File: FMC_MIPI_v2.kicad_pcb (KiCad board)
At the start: 6 copper layers, 69 x 112 mm, 99 parts, among them IC2 AT24MAC402-MAHM-T, IC3 TCA9406DCUR, J1 ASP-134488-01, J2 QTH-060-01-L-D-A, U1 LP5907MFX-1.8, U2 SN74AVC2T45DCUR, U3 SN74AVCH16T245_DGV_48, U4 TLV75525PDBV, U5 TS3DDR3812_RUA_42, U6 TS3DDR3812_RUA_42, U7 LP5907MFX-1.2, U8 SN74AVCH16T245_DGV_48

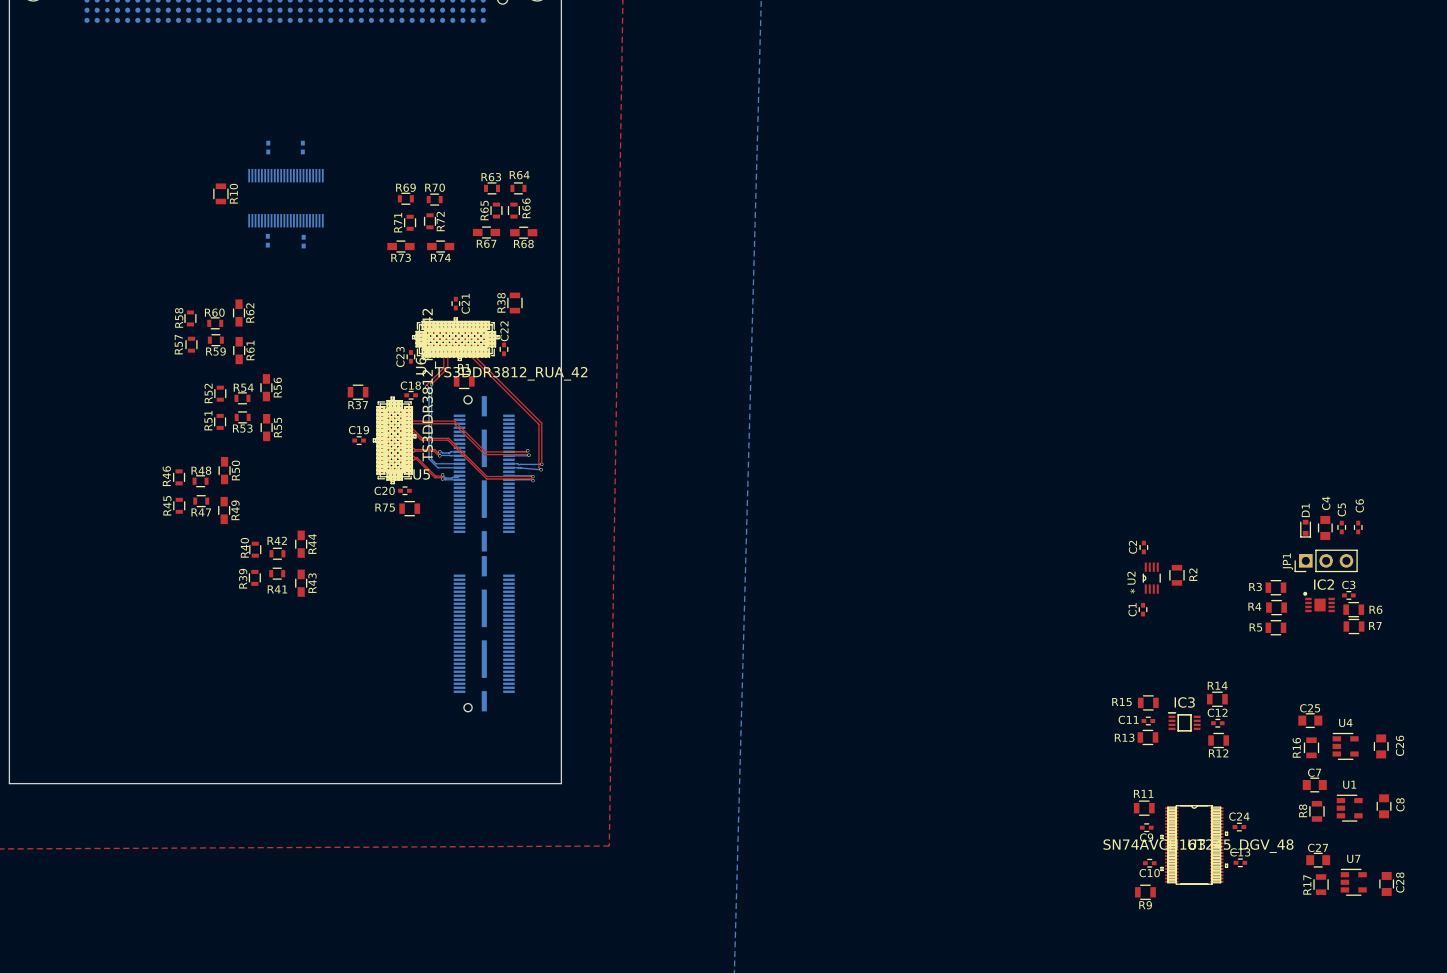
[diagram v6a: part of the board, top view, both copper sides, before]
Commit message: added 4 bit level shifter VADJ to 3.3 volt
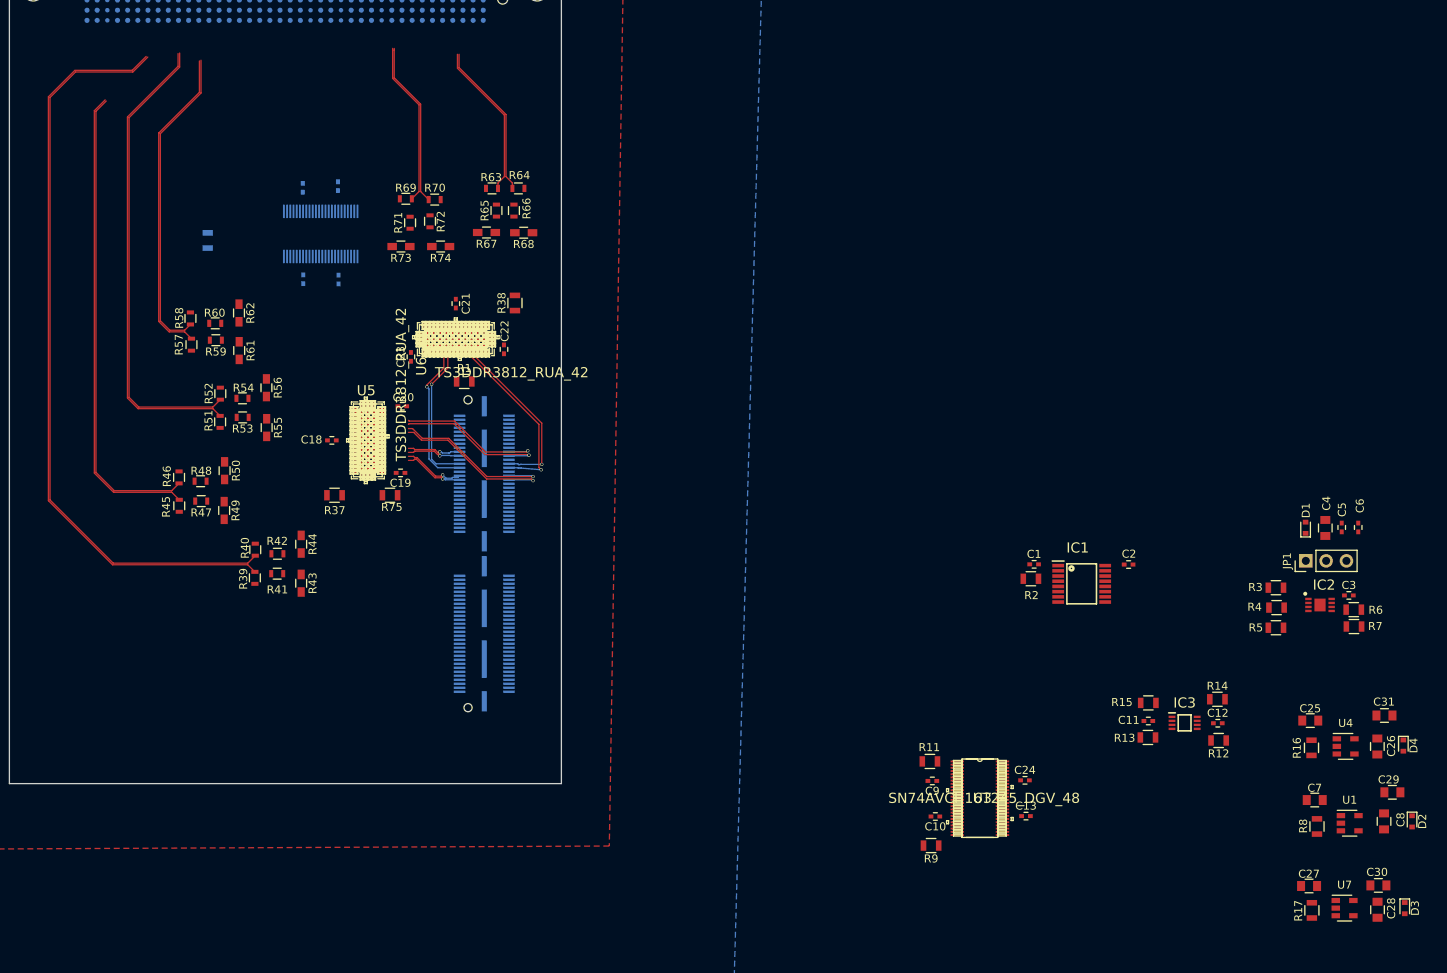
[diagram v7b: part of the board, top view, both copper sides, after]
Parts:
- removed U2: SN74AVC2T45DCUR, FMC_MIPI_v2_sym:SN74AVC2T45DCUR
- added C29: 4.7uF, Capacitors_SMD:C_0805, F.Cu at (263.4, 142.1)
- added C30: 4.7uF, Capacitors_SMD:C_0805, F.Cu at (261.6, 153.7)
- added C31: 4.7uF, Capacitors_SMD:C_0805, F.Cu at (262.4, 132.5)
- added D2: UCLAMP0501H.TCT, Diodes_SMD:D_SOD-523, F.Cu at (265.8, 145.7)
- added D3: UCLAMP0501H.TCT, Diodes_SMD:D_SOD-523, F.Cu at (264.9, 156.6)
- added D4: UCLAMP0501H.TCT, Diodes_SMD:D_SOD-523, F.Cu at (264.7, 136.2)
- added IC1: SN74AVC4T245PWR, SOP65P640X120-16N, F.Cu at (224.5, 116.0)
- R10: moved to B.Cu
- moved C10 27.4 mm to (206.2, 145.1)
- moved C24 27.4 mm to (217.4, 140.6)
- moved C9 27.4 mm to (205.9, 140.7)
- moved R11 27.4 mm to (205.6, 138.2)
- moved U3 27.4 mm to (211.8, 142.8)
- moved C13 27.4 mm to (217.6, 145.1)
- moved R9 27.4 mm to (205.7, 148.7)
- moved R2 18.3 mm to (218.2, 115.4), turned to 0 degrees
- moved C1 14.7 mm to (218.6, 113.6), turned to 0 degrees
- moved R37 13.2 mm to (131.1, 105.0), turned to 0 degrees
- moved C18 11.4 mm to (130.8, 98.1), turned to 0 degrees
- moved C20 10.6 mm to (139.6, 93.8), turned to 180 degrees
- moved C14 9.96 mm to (131.6, 66.3)
- moved C19 6.57 mm to (139.4, 102.2), turned to 180 degrees
- moved C16 6.54 mm to (127.2, 78.0)
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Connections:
- R2 pad 2: /LVDS_to_Jetson_lines/DIR_U2 -> /LVDS_to_Jetson_lines/DIR_IC1
- R37 pad 1: /LVDS_to_Jetson_lines/EN -> /LVDS_to_Jetson_lines/EN_U5
- R37 pad 2: /VOLT_3P3 -> /LVDS_to_Jetson_lines/EN_MIPI_OUT_DATA_3V3
- R38 pad 1: /LVDS_to_Jetson_lines/EN -> /LVDS_to_Jetson_lines/EN_U6
- R38 pad 2: /VOLT_3P3 -> /LVDS_to_Jetson_lines/EN_MIPI_OUT_CLOCK_3V3
- U5 pad 8: /LVDS_to_Jetson_lines/EN -> /LVDS_to_Jetson_lines/EN_U5
- U6 pad 8: /LVDS_to_Jetson_lines/EN -> /LVDS_to_Jetson_lines/EN_U6
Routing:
- net /LVDS_to_Jetson_lines/FMC_HS_CSI_C_D1_N: track 0.00 -> 94.3 mm
- net /LVDS_to_Jetson_lines/FMC_HS_CSI_C_D1_P: track 0.00 -> 93.9 mm
- net /LVDS_to_Jetson_lines/FMC_HS_CSI_C_D0_N: track 0.00 -> 59.2 mm
- net /LVDS_to_Jetson_lines/FMC_HS_CSI_C_D0_P: track 0.00 -> 58.7 mm
- net /LVDS_to_Jetson_lines/FMC_HS_CSI_D_D1_N: track 0.00 -> 58.2 mm
- net /LVDS_to_Jetson_lines/FMC_HS_CSI_D_D1_P: track 0.00 -> 58.0 mm
- net /LVDS_to_Jetson_lines/FMC_HS_CSI_D_D0_N: track 0.00 -> 39.6 mm
- net /LVDS_to_Jetson_lines/FMC_HS_CSI_D_D0_P: track 0.00 -> 39.2 mm
- net /LVDS_to_Jetson_lines/FMC_HS_CSI_C_CLK_P: track 0.00 -> 20.7 mm
- net /LVDS_to_Jetson_lines/FMC_HS_CSI_C_CLK_N: track 0.00 -> 20.5 mm
- net /LVDS_to_Jetson_lines/FMC_HS_CSI_D_CLK_P: track 0.00 -> 19.5 mm
- net /LVDS_to_Jetson_lines/FMC_HS_CSI_D_CLK_N: track 0.00 -> 19.5 mm

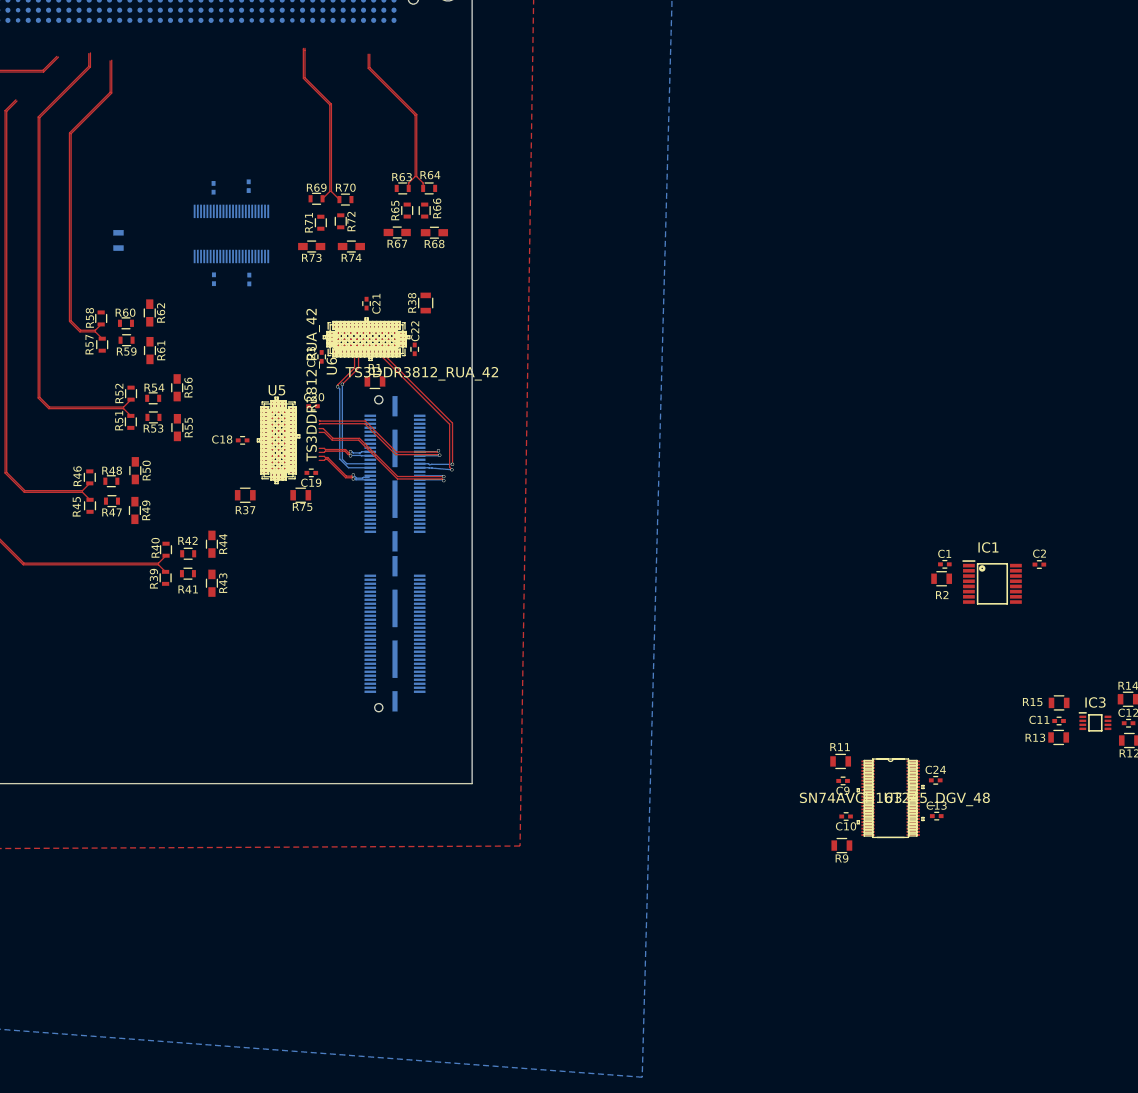
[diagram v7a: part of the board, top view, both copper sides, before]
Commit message: added enable line for slow signals
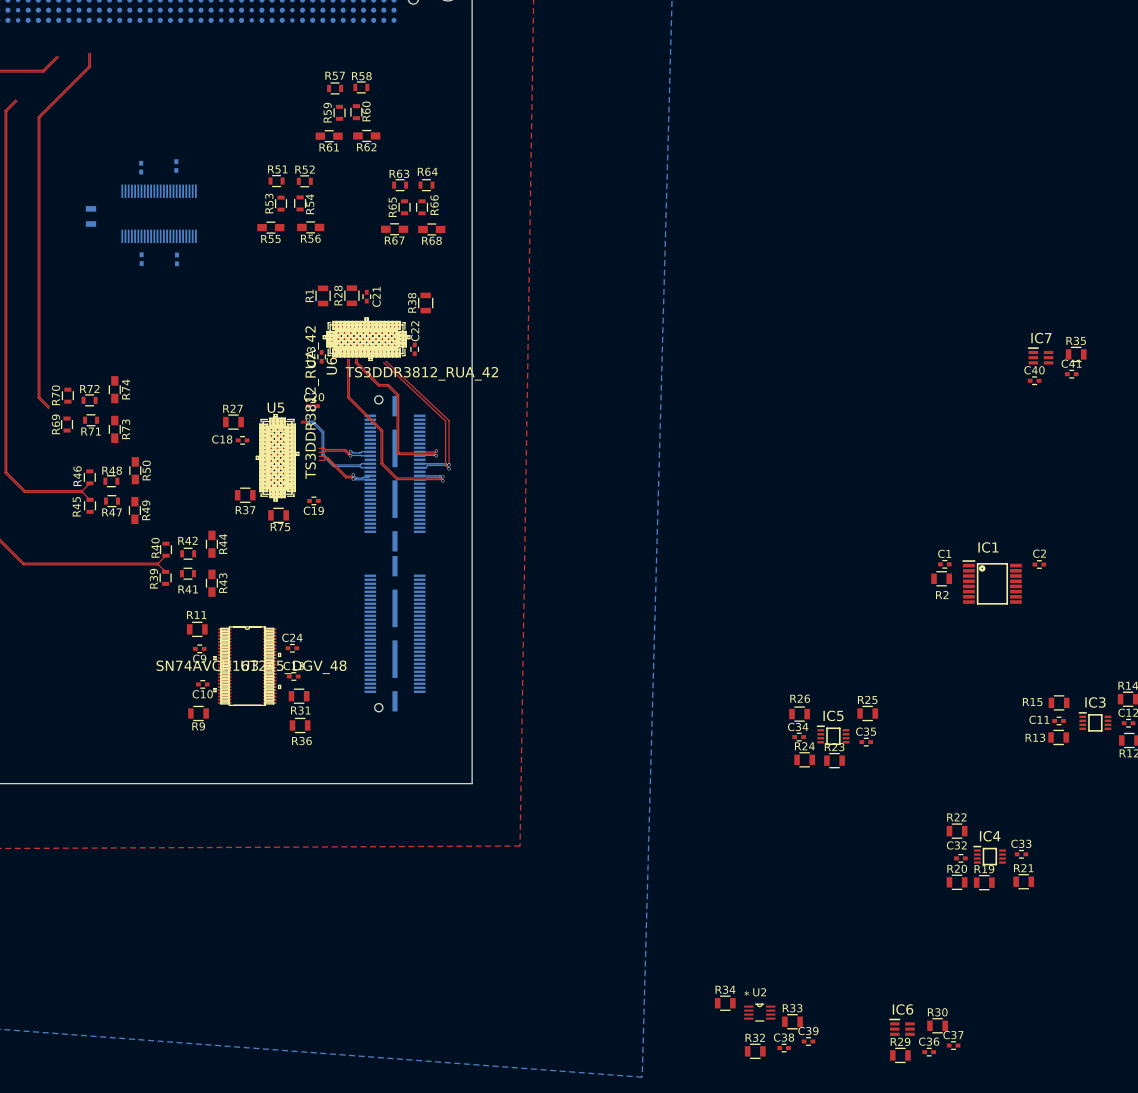
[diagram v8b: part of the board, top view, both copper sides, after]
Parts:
- added C32: 0.1uF, Capacitors_SMD:C_0402, F.Cu at (220.6, 150.3)
- added C33: 0.1uF, Capacitors_SMD:C_0402, F.Cu at (228.2, 149.8)
- added C34: 0.1uF, Capacitors_SMD:C_0402, F.Cu at (200.4, 135.2)
- added C35: 0.1uF, Capacitors_SMD:C_0402, F.Cu at (208.8, 135.8)
- added C36: 0.1uF, Capacitors_SMD:C_0402, F.Cu at (216.6, 174.6)
- added C37: 0.1uF, Capacitors_SMD:C_0402, F.Cu at (219.7, 173.7)
- added C38: 0.1uF, Capacitors_SMD:C_0402, F.Cu at (198.5, 174.1)
- added C39: 0.1uF, Capacitors_SMD:C_0402, F.Cu at (201.5, 173.2)
- added C40: 0.1uF, Capacitors_SMD:C_0402, F.Cu at (229.8, 90.6)
- added C41: 0.1uF, Capacitors_SMD:C_0402, F.Cu at (234.5, 89.8)
- added IC4: TCA9406DCUR, FMC_MIPI_v2_sym:SOP50P310X90-8N, F.Cu at (224.2, 150.1)
- added IC5: TCA9406DCUR, FMC_MIPI_v2_sym:SOP50P310X90-8N, F.Cu at (204.7, 135.1)
- added IC6: SN74AVC1T45DCKT, FMC_MIPI_v2_sym:SOT65P210X110-6N, F.Cu at (213.3, 171.7)
- added IC7: SN74AVC1T45DCKT, FMC_MIPI_v2_sym:SOT65P210X110-6N, F.Cu at (230.6, 87.8)
- added R19: 0, Resistors_SMD:R_0805, F.Cu at (223.5, 153.4)
- added R20: 0, Resistors_SMD:R_0805, F.Cu at (220.1, 153.3)
- added R21: 0, Resistors_SMD:R_0805, F.Cu at (228.4, 153.3)
- added R22: 0, Resistors_SMD:R_0805, F.Cu at (220.1, 146.9)
- added R23: 0, Resistors_SMD:R_0805, F.Cu at (204.8, 138.1)
- added R24: 0, Resistors_SMD:R_0805, F.Cu at (201.1, 138.0)
- added R25: 0, Resistors_SMD:R_0805, F.Cu at (208.9, 132.2)
- added R26: 0, Resistors_SMD:R_0805, F.Cu at (200.4, 132.3)
- added R27: 0, Resistors_SMD:R_0805, F.Cu at (129.7, 95.8)
- added R28: 0, Resistors_SMD:R_0805, F.Cu at (144.5, 80.0)
- added R29: 1k, Resistors_SMD:R_0805, F.Cu at (213.0, 175.0)
- added R30: 4.7k, Resistors_SMD:R_0805, F.Cu at (217.7, 171.3)
- added R31: 1k, Resistors_SMD:R_0805, F.Cu at (137.9, 130.1)
- added R32: 1k, Resistors_SMD:R_0805, F.Cu at (194.9, 174.5)
- added R33: 4.7k, Resistors_SMD:R_0805, F.Cu at (199.5, 170.8)
- added R34: 1k, Resistors_SMD:R_0805, F.Cu at (191.1, 168.5)
- added R35: 4.7k, Resistors_SMD:R_0805, F.Cu at (235.0, 87.4)
- added R36: 0, Resistors_SMD:R_0805, F.Cu at (138.0, 133.7)
- added U2: SN74AVC2T45DCUR, FMC_MIPI_v2_sym:SN74AVC2T45DCUR, F.Cu at (195.5, 169.6)
- moved C13 82.2 mm to (137.2, 127.6)
- moved C24 82.1 mm to (137.0, 124.1)
- moved C10 82.1 mm to (125.8, 128.6)
- moved C9 82.1 mm to (125.5, 124.2)
- moved R11 82.1 mm to (125.1, 121.7)
- moved R9 82.1 mm to (125.3, 132.2)
- moved U3 82.1 mm to (131.4, 126.3)
- moved R58 43.5 mm to (145.6, 54.0), turned to 180 degrees
- moved R57 43.3 mm to (142.4, 54.1), turned to 180 degrees
- moved R70 42.5 mm to (109.0, 92.5), turned to 270 degrees
- moved R69 42.1 mm to (108.9, 96.1), turned to 270 degrees
- moved R60 39.1 mm to (145.0, 57.1), turned to 90 degrees
- moved R59 38.9 mm to (142.9, 57.1), turned to 90 degrees
- moved R72 38.6 mm to (111.7, 93.1), turned to 180 degrees
- moved R71 37.9 mm to (111.9, 95.6), turned to 180 degrees
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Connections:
- net /LVDS_to_Jetson_lines/EN_MIPI_OUT_CLOCK_3V3 renamed /LVDS_to_Jetson_lines/EN_MIPI_OUT_CSI_D
- net /LVDS_to_Jetson_lines/EN_MIPI_OUT_DATA_3V3 renamed /LVDS_to_Jetson_lines/EN_MIPI_OUT_CSI_C
- C4 pad 2: /Jetson_connector/VCC_1V8_EEPROM -> JT_VDD_1V8
- C5 pad 2: /Jetson_connector/VCC_1V8_EEPROM -> JT_VDD_1V8
- C6 pad 2: /Jetson_connector/VCC_1V8_EEPROM -> JT_VDD_1V8
- D1 pad 1: /Jetson_connector/VCC_1V8_EEPROM -> JT_VDD_1V8
- IC1 pad 12: /LVDS_to_Jetson_lines/SWITCH_CLOCK_LANES_3V3 -> /LVDS_to_Jetson_lines/SWITCH_CLOCK_LANES_CSI_CD
- IC1 pad 13: /LVDS_to_Jetson_lines/SWITCH_DATA_LANES_3V3 -> /LVDS_to_Jetson_lines/SWITCH_DATA_LANES_CSI_CD
- J2 pad 101: (no net) -> /Jetson_connector/JT_VDD_1V2
- J2 pad 102: /Jetson_connector/JT_VDD_1V8 -> JT_VDD_1V8
- J2 pad 105: (no net) -> JT_1p8V_I2C3_CAM_CLK
- J2 pad 107: (no net) -> JT_1p8V_I2C3_CAM_DAT
- J2 pad 81: (no net) -> /Jetson_connector/JT_VDD_2V8
- J2 pad 82: (no net) -> /Jetson_connector/JT_VDD_2V8
- J2 pad 83: (no net) -> /Jetson_connector/JT_VDD_2V8
- J2 pad 87: (no net) -> JT_1p8V_I2C2_CAM_CLK
- J2 pad 89: (no net) -> JT_1p8V_I2C2_CAM_DAT
- JP1 pad 3: /Jetson_connector/JT_VDD_1V8 -> JT_VDD_1V8
- R1 pad 1: /LVDS_to_Jetson_lines/SWITCH_U6 -> /LVDS_to_Jetson_lines/SWITCH1_U6
- R1 pad 2: /LVDS_to_Jetson_lines/SWITCH_CLOCK_LANES_3V3 -> /LVDS_to_Jetson_lines/SWITCH_DATA_LANES_CSI_CD
- R11 pad 2: Earth -> /VOLT_1P8
- R75 pad 1: /LVDS_to_Jetson_lines/SWITCH_U5 -> /LVDS_to_Jetson_lines/SWITCH1_U5
- R75 pad 2: /LVDS_to_Jetson_lines/SWITCH_DATA_LANES_3V3 -> /LVDS_to_Jetson_lines/SWITCH_DATA_LANES_CSI_CD
- R9 pad 2: /VOLT_1P8 -> Earth
- U3 pad 25: Earth -> Net-(R36-Pad1)
- U3 pad 29: (no net) -> JT_1p8V_GPIO17_IN
- U3 pad 30: JT_1p8V_CAM0_MCLK -> JT_1p8V_GPIO9_IN
- U3 pad 32: JT_1p8V_CAM0_RST -> (no net)
- U3 pad 33: JT_1p8V_CAM0_PWR -> (no net)
- U3 pad 41: (no net) -> Net-(R31-Pad1)
- U3 pad 43: (no net) -> JT_1p8V_CAM0_RST
- U3 pad 44: (no net) -> JT_1p8V_CAM0_PWR
- U3 pad 46: JT_1p8V_GPIO9_IN -> (no net)
- U3 pad 47: JT_1p8V_GPIO17_IN -> JT_1p8V_CAM0_MCLK
- U5 pad 10: /LVDS_to_Jetson_lines/SWITCH_U5 -> /LVDS_to_Jetson_lines/SWITCH2_U5
- U5 pad 11: CSI_D_D1_N -> (no net)
- U5 pad 12: CSI_D_D1_P -> (no net)
- U5 pad 13: CSI_D_D0_N -> CSI_C_CLK_N
- U5 pad 14: CSI_D_D0_P -> CSI_C_CLK_P
- U5 pad 22: /LVDS_to_Jetson_lines/LP_CSI_D_D0_P -> /LVDS_to_Jetson_lines/LP_CSI_C_CLK_P
- U5 pad 23: /LVDS_to_Jetson_lines/HS_CSI_D_D0_P -> /LVDS_to_Jetson_lines/HS_CSI_C_CLK_P
- U5 pad 24: /LVDS_to_Jetson_lines/LP_CSI_D_D0_N -> /LVDS_to_Jetson_lines/LP_CSI_C_CLK_N
- U5 pad 25: /LVDS_to_Jetson_lines/HS_CSI_D_D0_N -> /LVDS_to_Jetson_lines/HS_CSI_C_CLK_N
- U5 pad 26: /LVDS_to_Jetson_lines/LP_CSI_D_D1_P -> (no net)
- U5 pad 27: /LVDS_to_Jetson_lines/HS_CSI_D_D1_P -> (no net)
- U5 pad 28: /LVDS_to_Jetson_lines/LP_CSI_D_D1_N -> (no net)
- U5 pad 29: /LVDS_to_Jetson_lines/HS_CSI_D_D1_N -> (no net)
- U5 pad 9: /LVDS_to_Jetson_lines/SWITCH_U5 -> /LVDS_to_Jetson_lines/SWITCH1_U5
- U6 pad 10: /LVDS_to_Jetson_lines/SWITCH_U6 -> /LVDS_to_Jetson_lines/SWITCH2_U6
- U6 pad 31: /LVDS_to_Jetson_lines/LP_CSI_C_CLK_P -> /LVDS_to_Jetson_lines/LP_CSI_D_D0_P
- U6 pad 32: /LVDS_to_Jetson_lines/HS_CSI_C_CLK_P -> /LVDS_to_Jetson_lines/HS_CSI_D_D0_P
- U6 pad 33: /LVDS_to_Jetson_lines/LP_CSI_C_CLK_N -> /LVDS_to_Jetson_lines/LP_CSI_D_D0_N
- U6 pad 34: /LVDS_to_Jetson_lines/HS_CSI_C_CLK_N -> /LVDS_to_Jetson_lines/HS_CSI_D_D0_N
- U6 pad 35: (no net) -> /LVDS_to_Jetson_lines/LP_CSI_D_D1_P
- U6 pad 36: (no net) -> /LVDS_to_Jetson_lines/HS_CSI_D_D1_P
- U6 pad 37: (no net) -> /LVDS_to_Jetson_lines/LP_CSI_D_D1_N
- U6 pad 38: (no net) -> /LVDS_to_Jetson_lines/HS_CSI_D_D1_N
- U6 pad 4: (no net) -> CSI_D_D1_N
- U6 pad 5: (no net) -> CSI_D_D1_P
- U6 pad 6: CSI_C_CLK_N -> CSI_D_D0_N
- U6 pad 7: CSI_C_CLK_P -> CSI_D_D0_P
- U6 pad 9: /LVDS_to_Jetson_lines/SWITCH_U6 -> /LVDS_to_Jetson_lines/SWITCH1_U6
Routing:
- net /LVDS_to_Jetson_lines/FMC_HS_CSI_D_D0_N: track 39.6 -> 0.00 mm
- net /LVDS_to_Jetson_lines/FMC_HS_CSI_D_D0_P: track 39.2 -> 0.00 mm
- net /LVDS_to_Jetson_lines/FMC_HS_CSI_C_CLK_P: track 20.7 -> 0.00 mm
- net /LVDS_to_Jetson_lines/FMC_HS_CSI_C_CLK_N: track 20.5 -> 0.00 mm
- net /LVDS_to_Jetson_lines/FMC_HS_CSI_D_CLK_P: track 19.5 -> 0.00 mm
- net /LVDS_to_Jetson_lines/FMC_HS_CSI_D_CLK_N: track 19.5 -> 0.00 mm
- net /LVDS_to_Jetson_lines/FMC_HS_CSI_D_D1_N: track 58.2 -> 47.6 mm
- net /LVDS_to_Jetson_lines/FMC_HS_CSI_D_D1_P: track 58.0 -> 47.4 mm
- net CSI_C_CLK_N: track 18.5 -> 12.8 mm
- net CSI_D_D1_N: track 21.1 -> 26.6 mm
- net CSI_C_CLK_P: track 17.9 -> 12.7 mm
- net CSI_D_D1_P: track 21.1 -> 26.0 mm
- net CSI_D_D0_P: track 19.0 -> 21.5 mm
- net CSI_D_D0_N: track 19.3 -> 21.7 mm
- net CSI_D_CLK_P: track 21.5 -> 20.1 mm
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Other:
- board text removed: "HS Clocks here"
